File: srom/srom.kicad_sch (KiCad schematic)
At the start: 14 parts, among them J1 Conn_01x03_Female, Q1 PN2222A, U1 4075, U2 74LS245, U3 74LS245, U4 74LS245, U5 Pico-rp2040

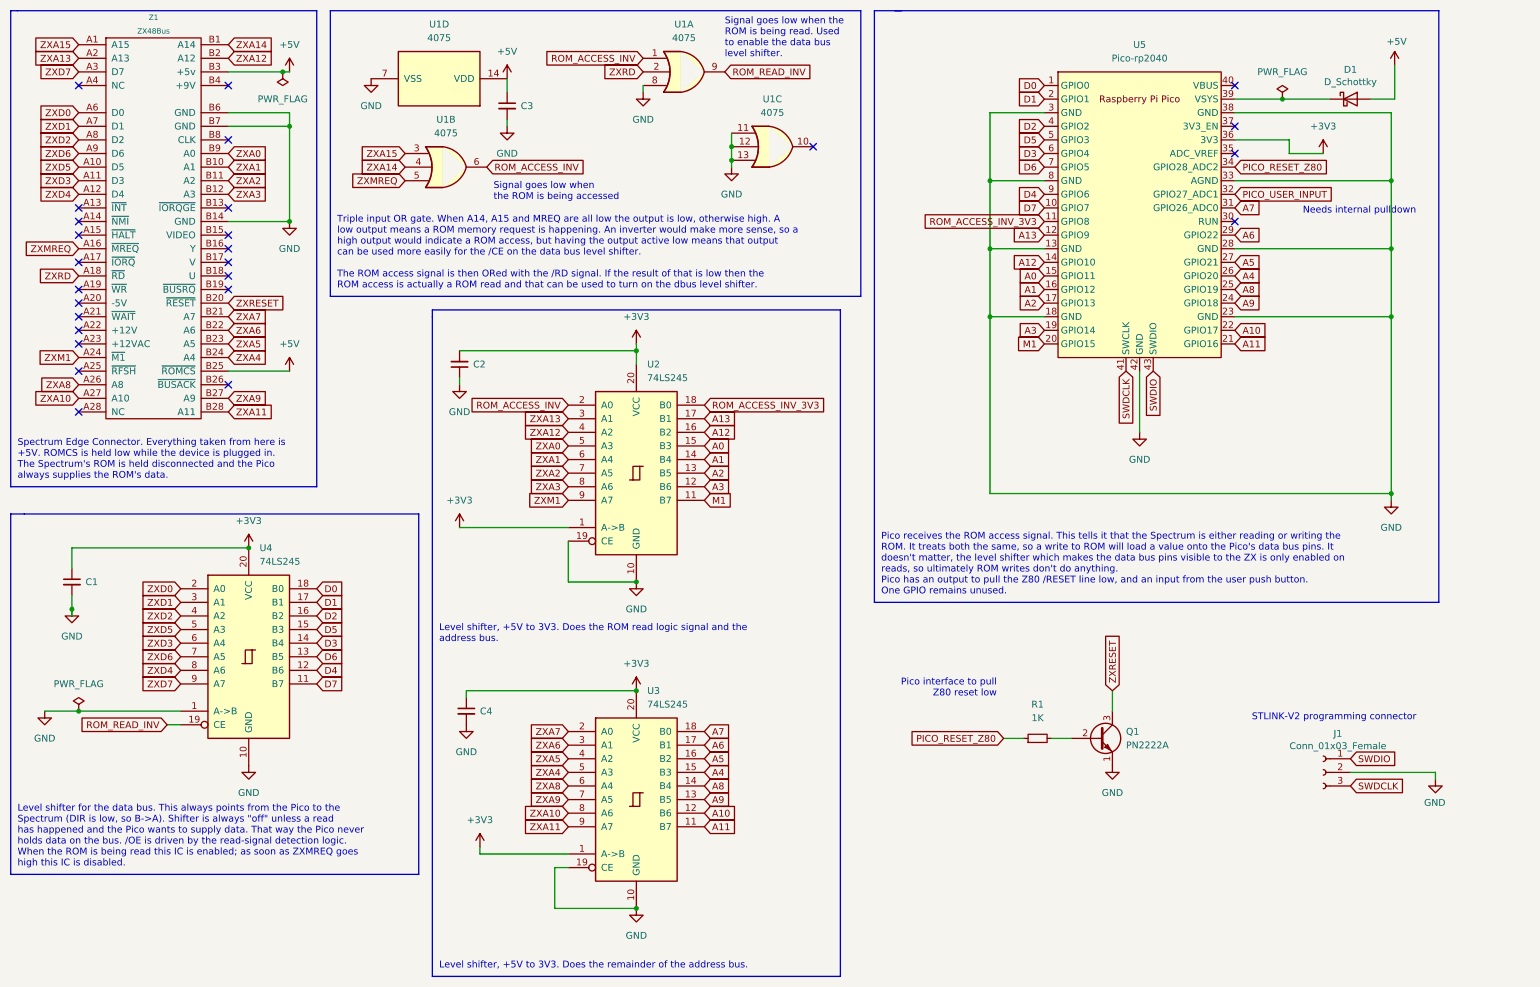
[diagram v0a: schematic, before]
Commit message: add IO and UI schematics
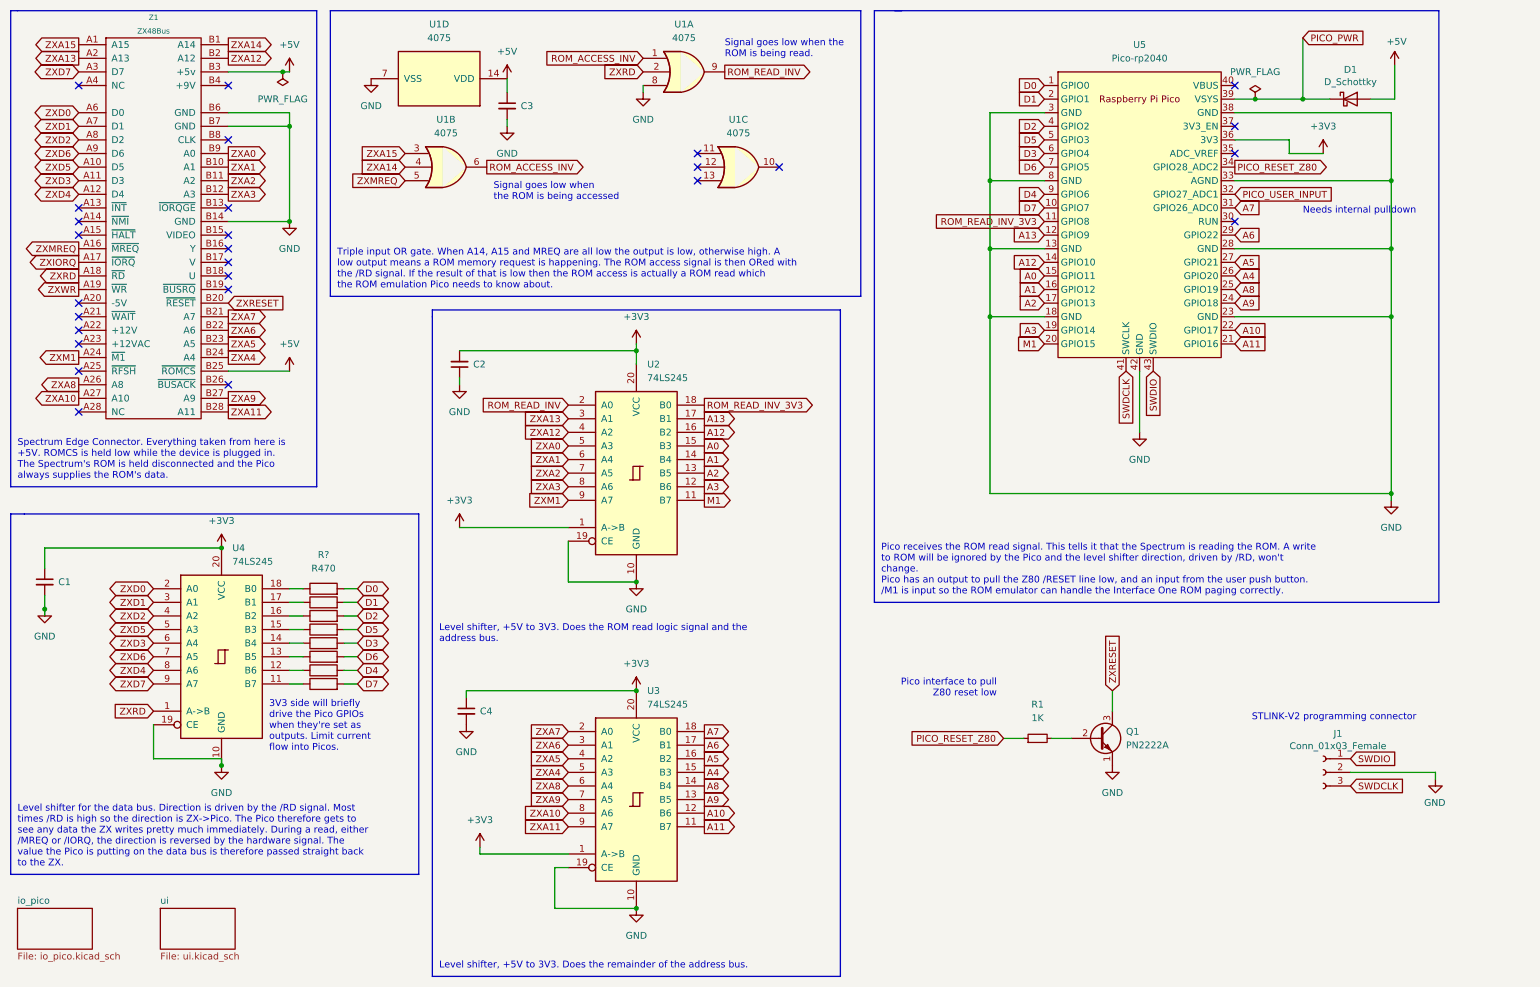
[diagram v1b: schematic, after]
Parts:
- added R? (x8): R470, symbol Device:R
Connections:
- net D0: now also R?.2; no longer U4.18 (B0)
- net D1: now also R?.2; no longer U4.17 (B1)
- net D2: now also R?.2; no longer U4.16 (B2)
- net D3: now also R?.2; no longer U4.14 (B4)
- net D4: now also R?.2; no longer U4.12 (B6)
- net D5: now also R?.2; no longer U4.15 (B3)
- net D6: now also R?.2; no longer U4.13 (B5)
- net D7: now also R?.2; no longer U4.11 (B7)
- net GND: now also U4.19 (CE); no longer U1.11, U1.12, U1.13, U4.1 (A->B)
- net ROM_ACCESS_INV: no longer U2.2 (A0)
- net ROM_READ_INV: now also U2.2 (A0); no longer U4.19 (CE)
- net ZXRD: now also U4.1 (A->B)
- net ZXIORQ: now reaches Z1.A17 (~{IORQ})
- net ZXWR: now reaches Z1.A19 (~{WR})
- net PICO_PWR: now reaches D1.1 (K), U5.39 (VSYS)
- net ROM_ACCESS_INV_3V3 renamed ROM_READ_INV_3V3
- new net: R?.1, U4.11 (B7)
- new net: R?.1, U4.12 (B6)
- new net: R?.1, U4.13 (B5)
- new net: R?.1, U4.14 (B4)
- new net: R?.1, U4.15 (B3)
- new net: R?.1, U4.16 (B2)
- new net: R?.1, U4.17 (B1)
- new net: R?.1, U4.18 (B0)
- no-connect marks 26 -> 27
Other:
- added sheet io_pico (io_pico.kicad_sch)
- added sheet ui (ui.kicad_sch)
- note added: "3V3 side will briefly drive the Pico GPIOs when they're set as outputs. Limit current flow into Picos."
- note added: "Level shifter for the data bus. Direction is driven by the /RD signal. Most times /RD is high so the direction is ZX->Pico. The Pico therefore gets to see any data the ZX writes pretty much immediately. During a read, either /MREQ or /IORQ, the direction is reversed by the hardware signal. The value the Pico is putting on the data bus is therefore passed straight back to the ZX."
- note added: "Pico receives the ROM read signal. This tells it that the Spectrum is reading the ROM. A write to ROM will be ignored by the Pico and the level shifter direction, driven by /RD, won't change. Pico has an output to pull the Z80 /RESET line low, and an input from the user push button. /M1 is input so the ROM emulator can handle the Interface One ROM paging correctly."
- note added: "Signal goes low when the ROM is being read."
- note added: "Triple input OR gate. When A14, A15 and MREQ are all low the output is low, otherwise high. A low output means a ROM memory request is happening. The ROM access signal is then ORed with the /RD signal. If the result of that is low then the ROM access is actually a ROM read which the ROM emulation Pico needs to know about."
- note removed: "Level shifter for the data bus. This always points from the Pico to the Spectrum (DIR is low, so B->A). Shifter is always "off" unless a read has happened and the Pico wants to supply data. That way the Pico never holds data on the bus. /OE is driven by the read-signal detection logic. When the ROM is being read this IC is enabled; as soon as ZXMREQ goes high this IC is disabled."
- note removed: "Pico receives the ROM access signal. This tells it that the Spectrum is either reading or writing the ROM. It treats both the same, so a write to ROM will load a value onto the Pico's data bus pins. It doesn't matter, the level shifter which makes the data bus pins visible to the ZX is only enabled on reads, so ultimately ROM writes don't do anything. Pico has an output to pull the Z80 /RESET lin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"
- note removed: "Signal goes low when the ROM is being read. Used to enable the data bus level shifter."
- note removed: "Triple input OR gate. When A14, A15 and MREQ are all low the output is low, otherwise high. A low output means a ROM memory request is happening. An inverter would make more sense, so a high output would indicate a ROM access, but having the output active low means that output can be used more easily for the /CE on the data bus level shifter. The ROM access signal is then ORed with the /RD signal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"
- moved on the sheet: C1, U1C, U4

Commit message: schematics complete for IO and UI picos
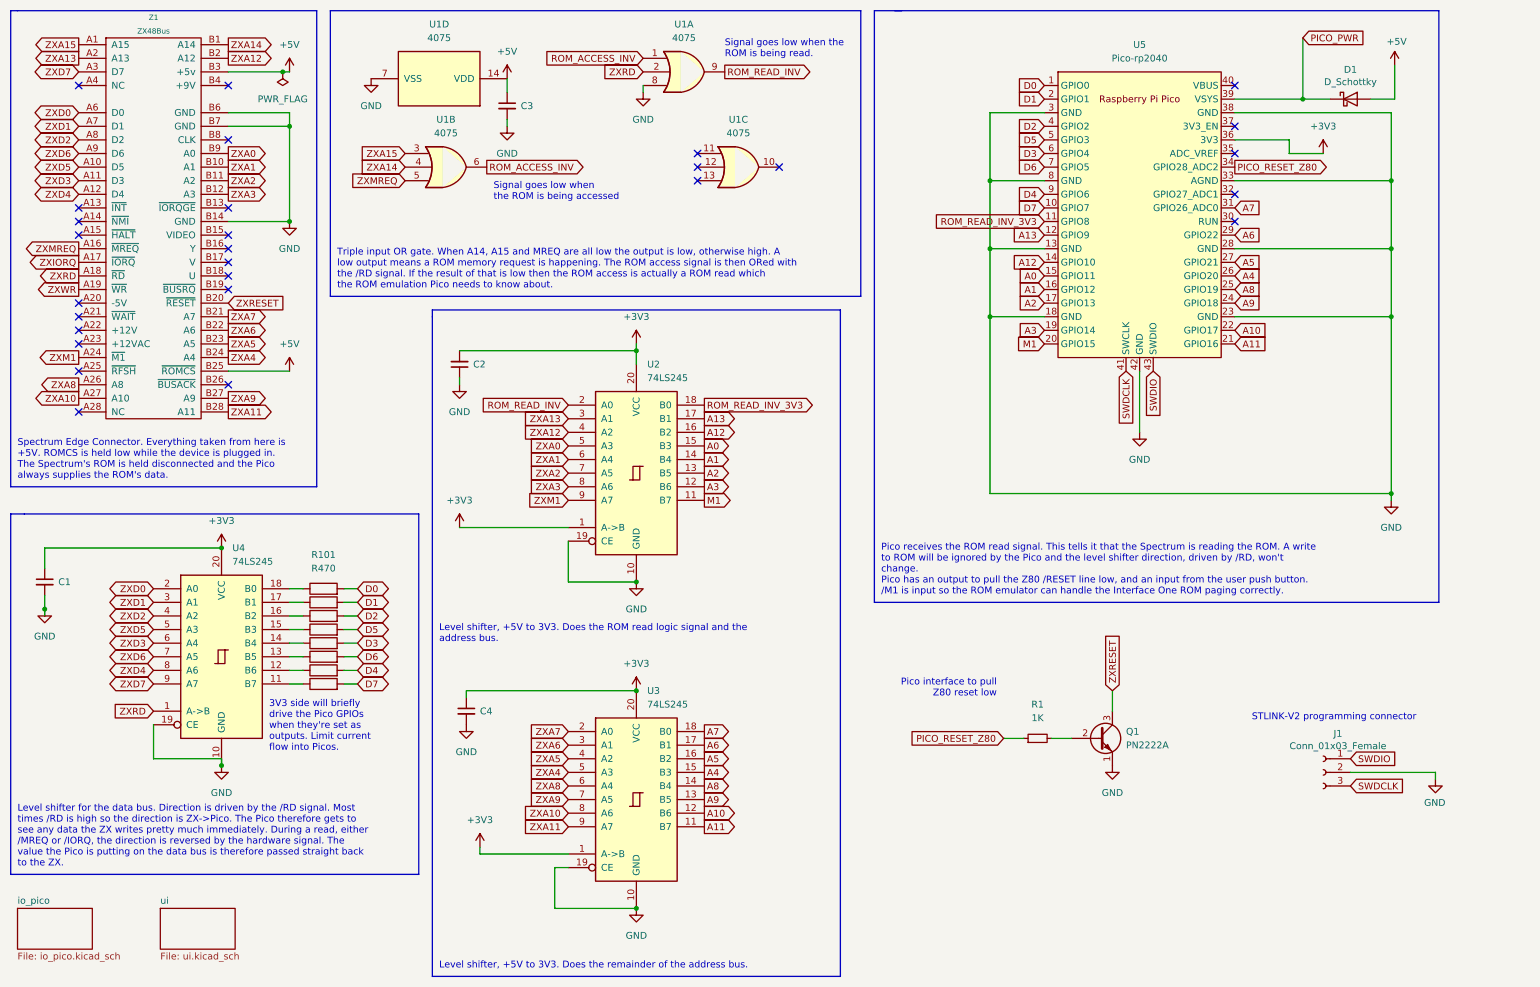
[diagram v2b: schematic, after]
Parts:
- gave numbers to parts that had none: 8
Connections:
- net PICO_USER_INPUT: no longer names the net of U5.32 (GPIO27_ADC1)
- no-connect marks 27 -> 28
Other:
- note removed: "Needs internal pulldown"

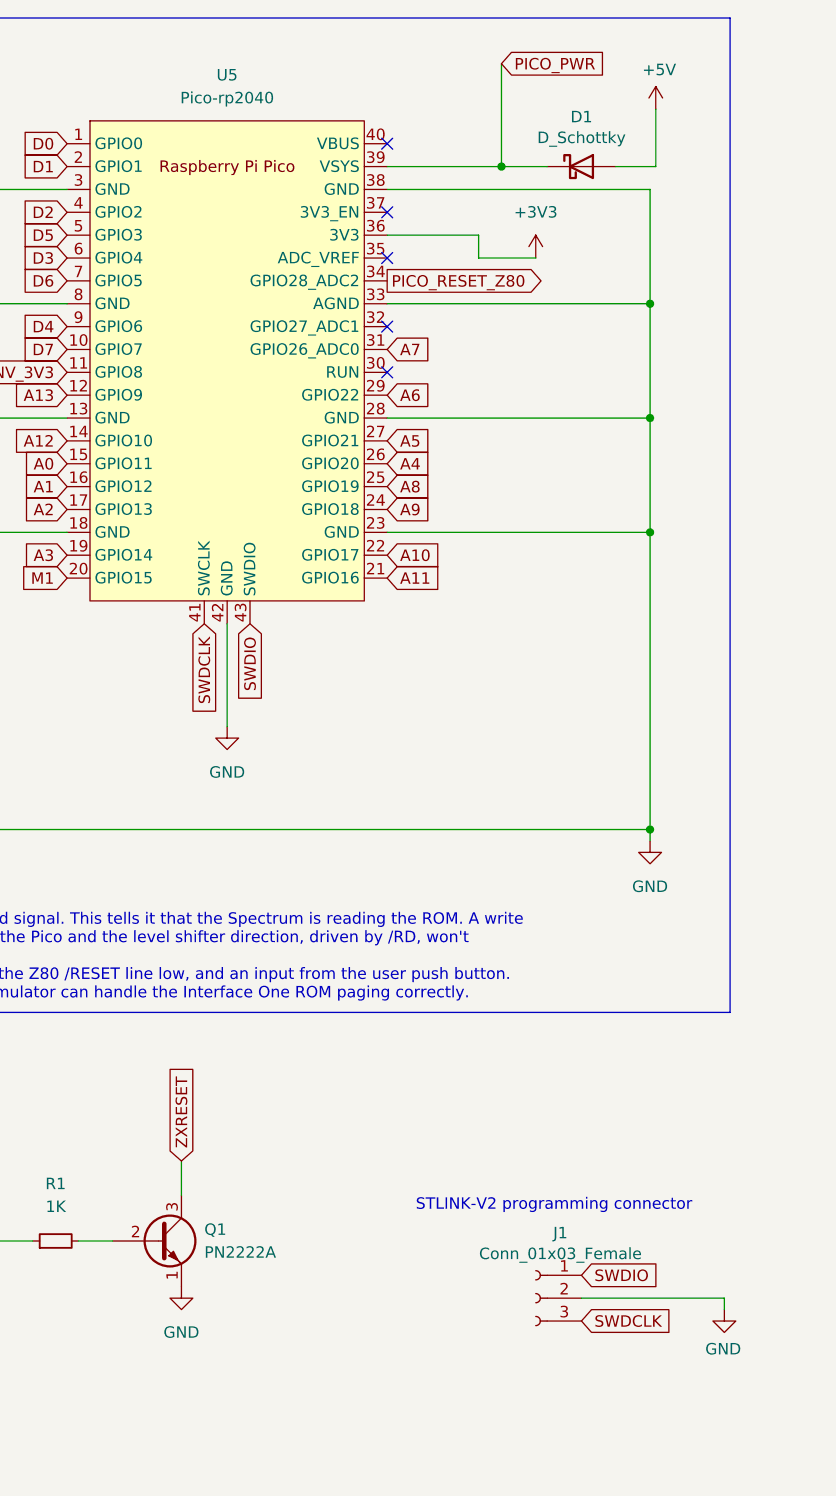
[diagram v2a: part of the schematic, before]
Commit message: first draft pcb layout
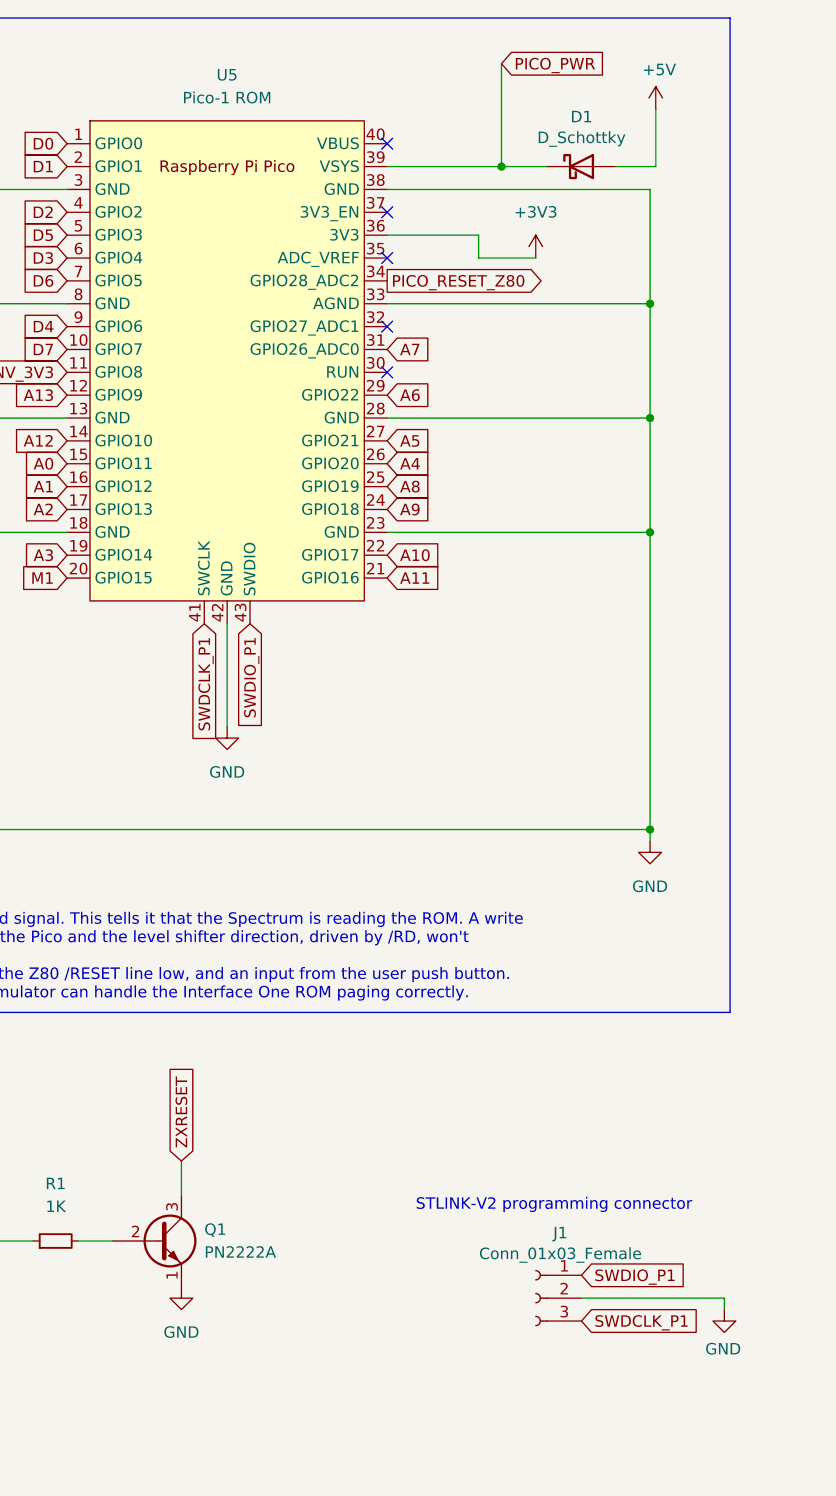
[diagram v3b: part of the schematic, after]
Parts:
- R101, R102, R103, R104, R105, R106, R107, R108: footprint (none) -> Resistor_SMD:R_1206_3216Metric_Pad1.30x1.75mm_HandSolder
- U5: value Pico-rp2040 -> Pico-1 ROM
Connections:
- net SWDCLK renamed SWDCLK_P1
- net SWDIO renamed SWDIO_P1

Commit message: ready for fab
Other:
- title: ZX Spectrum IF1 ROM -> Pico Interface One
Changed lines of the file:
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@@
   (paper "A4")
   (title_block
-    (title "ZX Spectrum IF1 ROM")
-    (date "2023-02-07")
+    (title "Pico Interface One")
+    (date "2023-02-12")
     (rev "1.0")
   )
